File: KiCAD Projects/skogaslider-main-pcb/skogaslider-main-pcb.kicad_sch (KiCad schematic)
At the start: 172 parts, among them J1 USB_C_Receptacle_USB2.0, J2 USB_C_Receptacle_USB2.0, J3 Conn_01x05, J4 Conn_02x16_Top_Bottom, J5 Conn_01x09, J6 Conn_01x09, J7 Conn_01x04, J8 Conn_01x04, Q1 BSS138, SW1 SW_Push, SW2 SW_Push, SW3 SW_Push, SW4 SW_Push, U1 AMS1117-3.3, U2 MPR121QR2, U3 MPR121QR2, U4 USBLC6-2P6, U5 RP2040, U6 M24C02-RMN, U7 W25Q128JVS, U8 MPR121QR2, U9 74HC4051, Y1 ABLS-12.000MHZ-B4-T

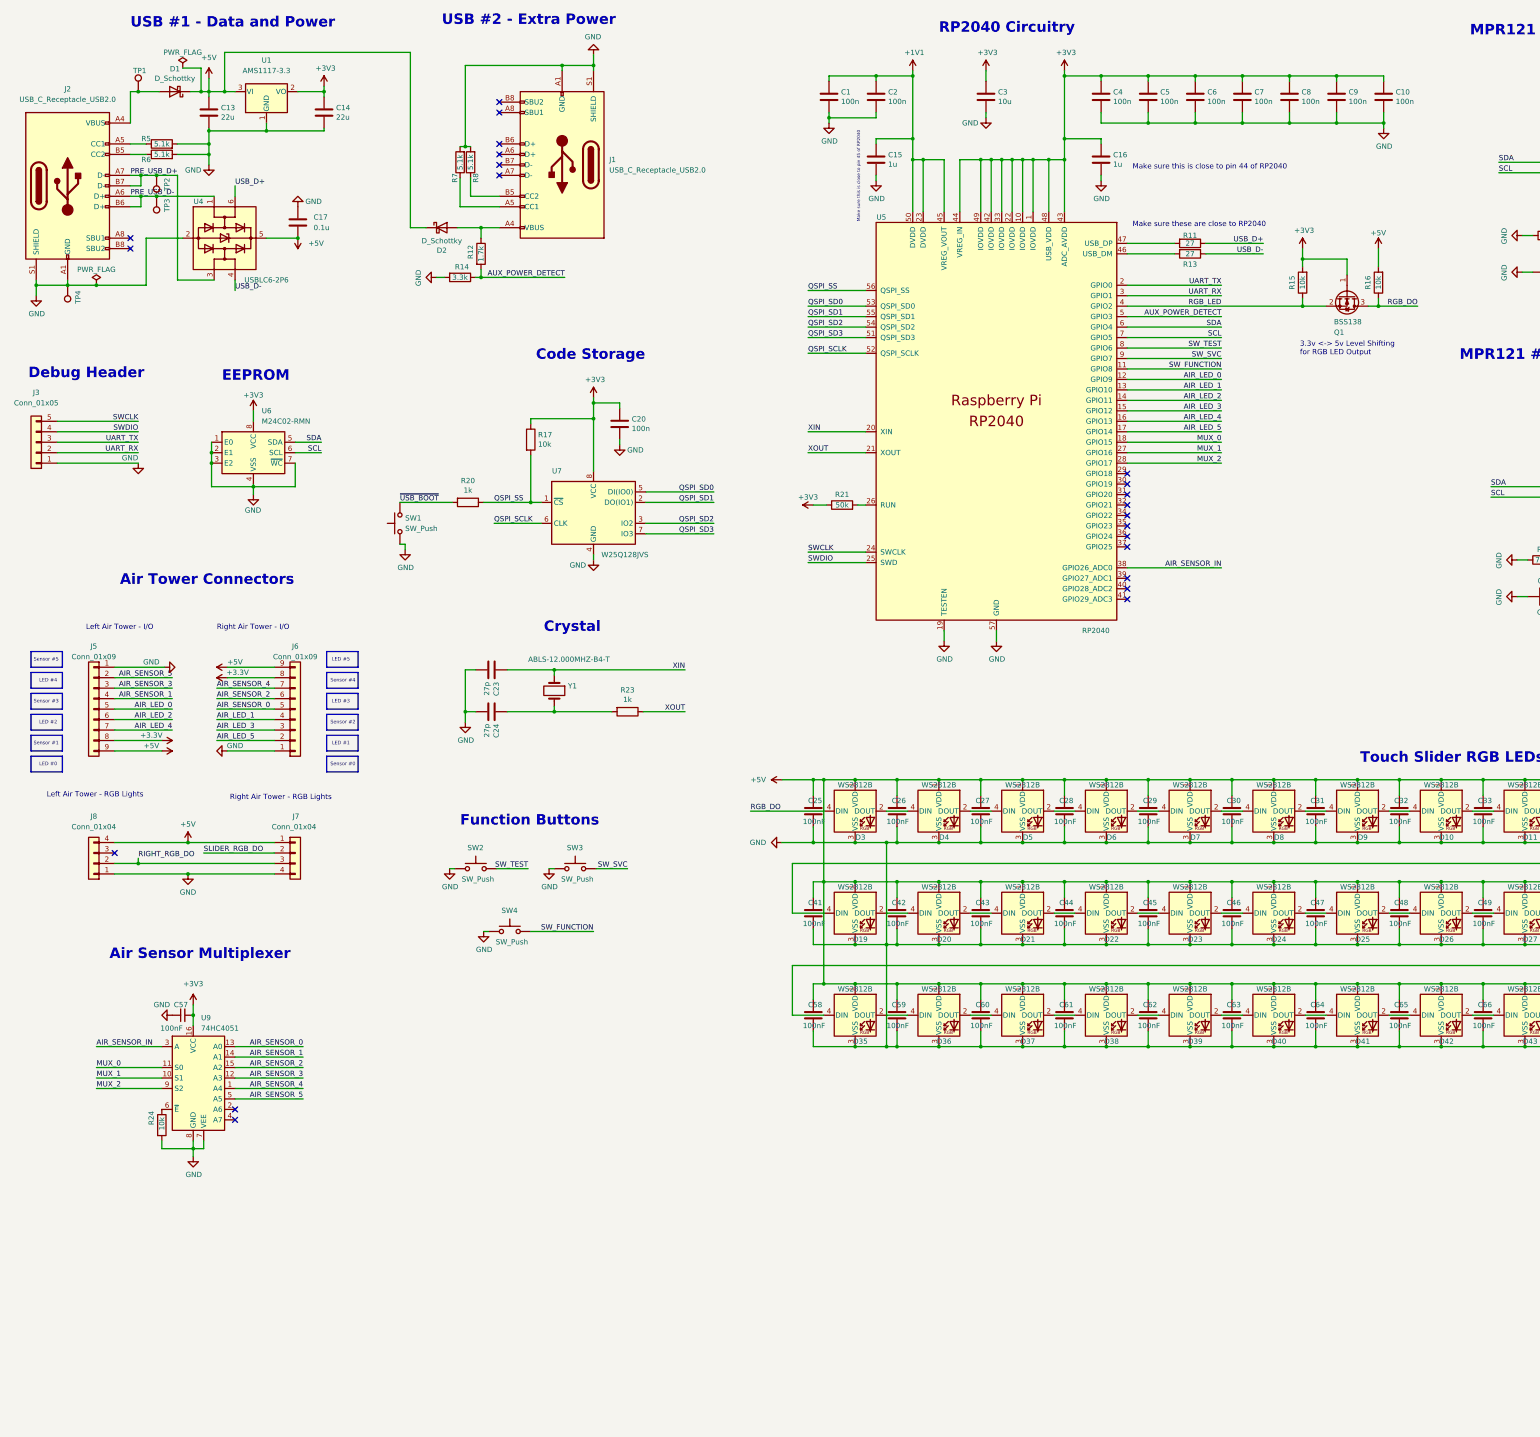
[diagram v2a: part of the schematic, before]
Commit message: PCB layout is almost complete for the mainboard, minus the board cuts, mounting holes, and power/ground planes
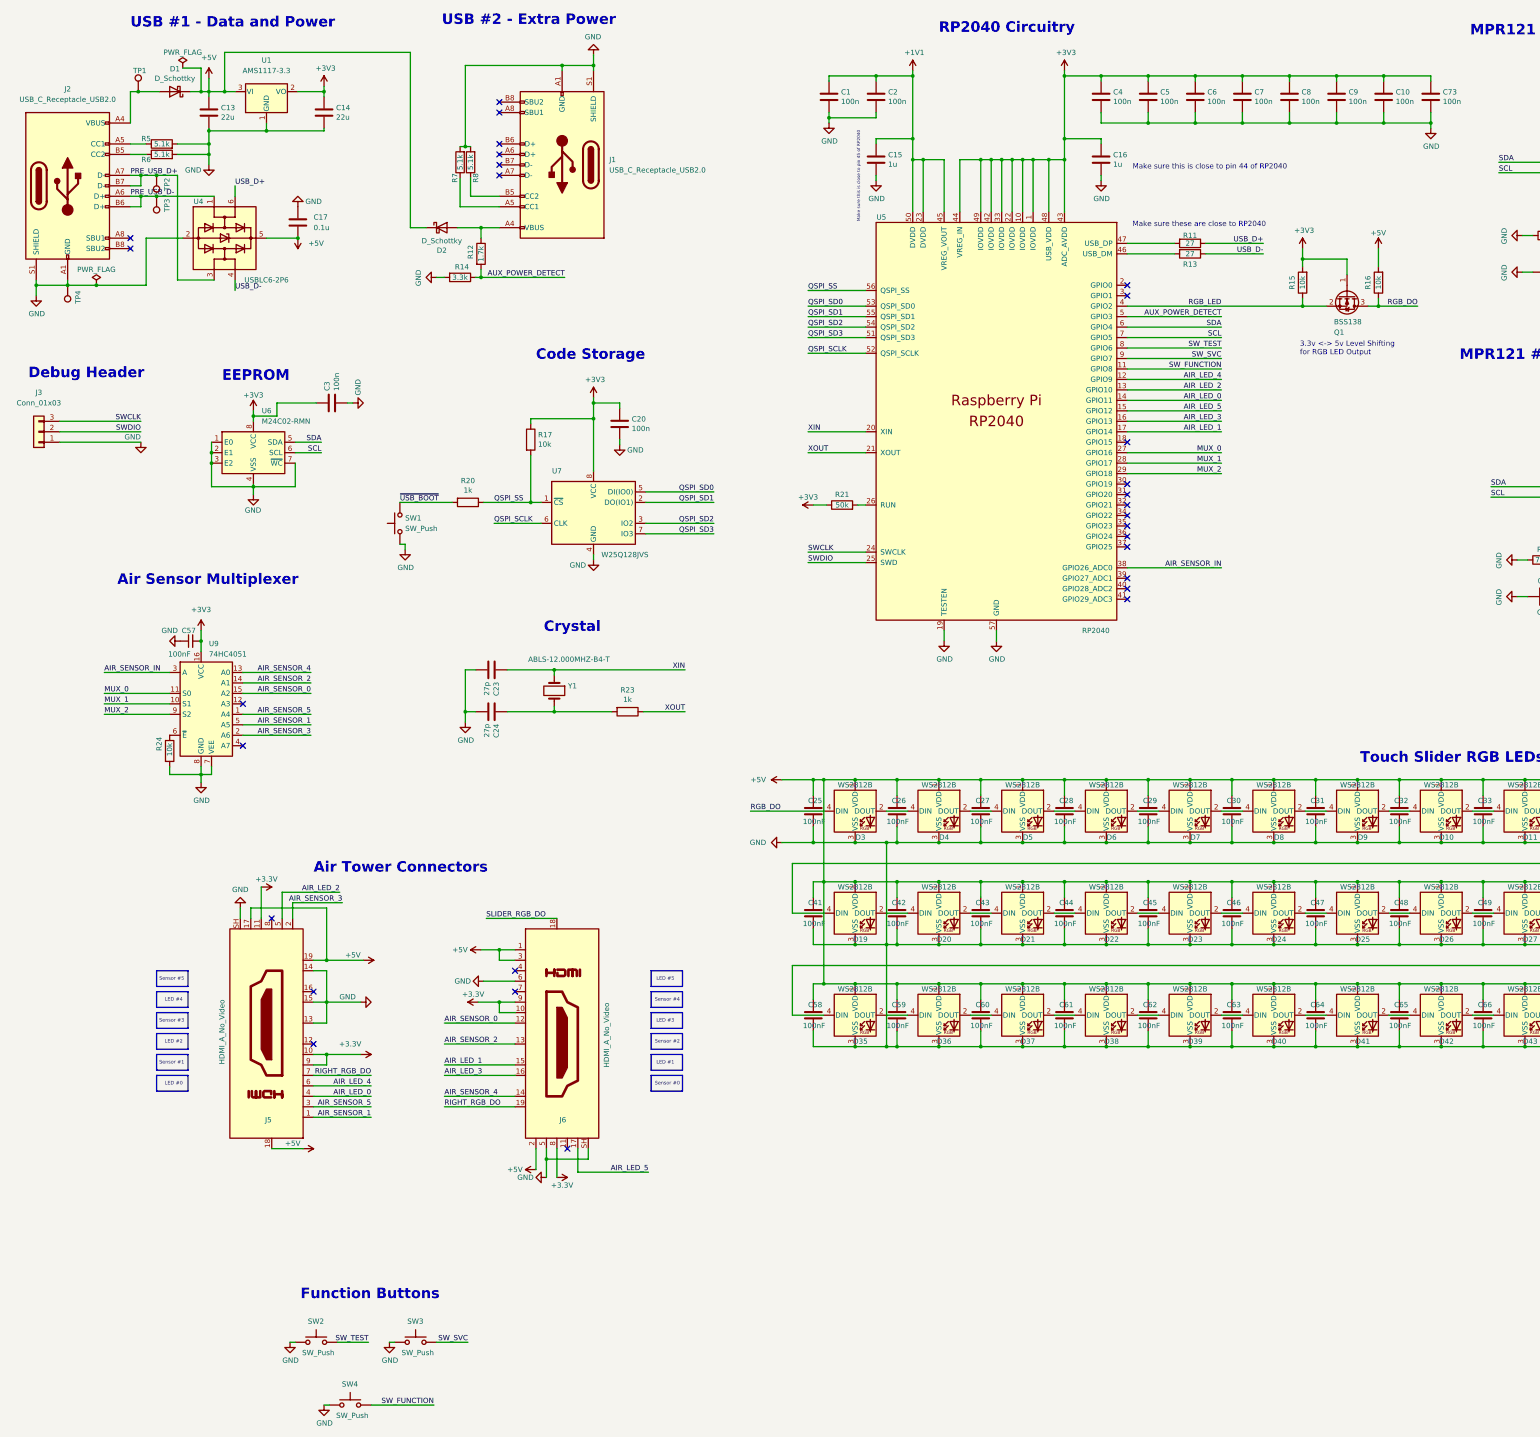
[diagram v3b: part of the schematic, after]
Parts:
- removed J3: Conn_01x05, Connector_PinHeader_2.54mm:PinHeader_1x05_P2.54mm_Vertical, symbol Connector_Generic:Conn_01x05
- removed J5, J6: Conn_01x09, Connector_JST:JST_PH_S9B-PH-K_1x09_P2.00mm_Horizontal, symbol Connector_Generic:Conn_01x09
- removed J7, J8: Conn_01x04, Connector_JST:JST_PH_S4B-PH-K_1x04_P2.00mm_Horizontal, symbol Connector_Generic:Conn_01x04
- added C73: 100n, Capacitor_SMD:C_0201_0603Metric, symbol Device:C
- added J3: Conn_01x03, Connector_PinHeader_2.54mm:PinHeader_1x03_P2.54mm_Vertical, symbol Connector_Generic:Conn_01x03
- added J5, J6: HDMI_A_No_Video, Skogaslider_Custom_Footprints:HDMI_Connector_SMD, symbol Skogaslider_Custom_Symbols:HDMI_A_No_Video
- C1, C10, C15, C16, C2, C4, C5, C6, C7, C8, C9: footprint Capacitor_SMD:C_0402_1005Metric -> Capacitor_SMD:C_0201_0603Metric
- C3: value 10u -> 100n; footprint Capacitor_SMD:C_0805_2012Metric -> Capacitor_SMD:C_0201_0603Metric
- R20: footprint Resistor_SMD:R_0402_1005Metric -> Resistor_SMD:R_0603_1608Metric
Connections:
- net +3V3: now also C73.1, J5.10, J5.11, J5.9, J6.10, J6.8, J6.9
- net +5V: now also J5.17, J5.18, J5.19, J6.1, J6.2, J6.3
- net AIR_LED_0: now also U5.14 (GPIO11), J5.4; no longer U5.12 (GPIO9)
- net AIR_LED_1: now also U5.17 (GPIO14), J6.15; no longer U5.13 (GPIO10)
- net AIR_LED_2: now also U5.13 (GPIO10), J5.5; no longer U5.14 (GPIO11)
- net AIR_LED_3: now also U5.16 (GPIO13), J6.16; no longer U5.15 (GPIO12)
- net AIR_LED_4: now also U5.12 (GPIO9), J5.6; no longer U5.16 (GPIO13)
- net AIR_LED_5: now also U5.15 (GPIO12), J6.17; no longer U5.17 (GPIO14)
- net AIR_SENSOR_0: now also U9.15 (A2), J6.12; no longer U9.13 (A0)
- net AIR_SENSOR_1: now also U9.5 (A5), J5.1; no longer U9.14 (A1)
- net AIR_SENSOR_2: now also U9.14 (A1), J6.13; no longer U9.15 (A2)
- net AIR_SENSOR_3: now also U9.2 (A6), J5.2; no longer U9.12 (A3)
- net AIR_SENSOR_4: now also U9.13 (A0), J6.14; no longer U9.1 (A4)
- net AIR_SENSOR_5: now also U9.1 (A4), J5.3; no longer U9.5 (A5)
- net GND: now also C73.2, J3.1 (Pin_1), J5.13, J5.14, J5.15, J5.SH, J6.5, J6.6, J6.SH
- net MUX_0: now also U5.27 (GPIO16); no longer U5.18 (GPIO15)
- net MUX_1: now also U5.28 (GPIO17); no longer U5.27 (GPIO16)
- net MUX_2: now also U5.29 (GPIO18); no longer U5.28 (GPIO17)
- net RIGHT_RGB_DO: now also J5.7, J6.19
- net SLIDER_RGB_DO: now also J6.18
- net SWCLK: now also J3.3 (Pin_3)
- net SWDIO: now also J3.2 (Pin_2)
- net UART_RX: no longer names the net of U5.3 (GPIO1)
- net UART_TX: no longer names the net of U5.2 (GPIO0)
- no-connect marks 29 -> 36
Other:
- note removed: "Left Air Tower - I/O"
- note removed: "Left Air Tower - RGB Lights"
- note removed: "Right Air Tower - I/O"
- note removed: "Right Air Tower - RGB Lights"
- moved on the sheet: C57, R24, SW2, SW3, SW4, U9

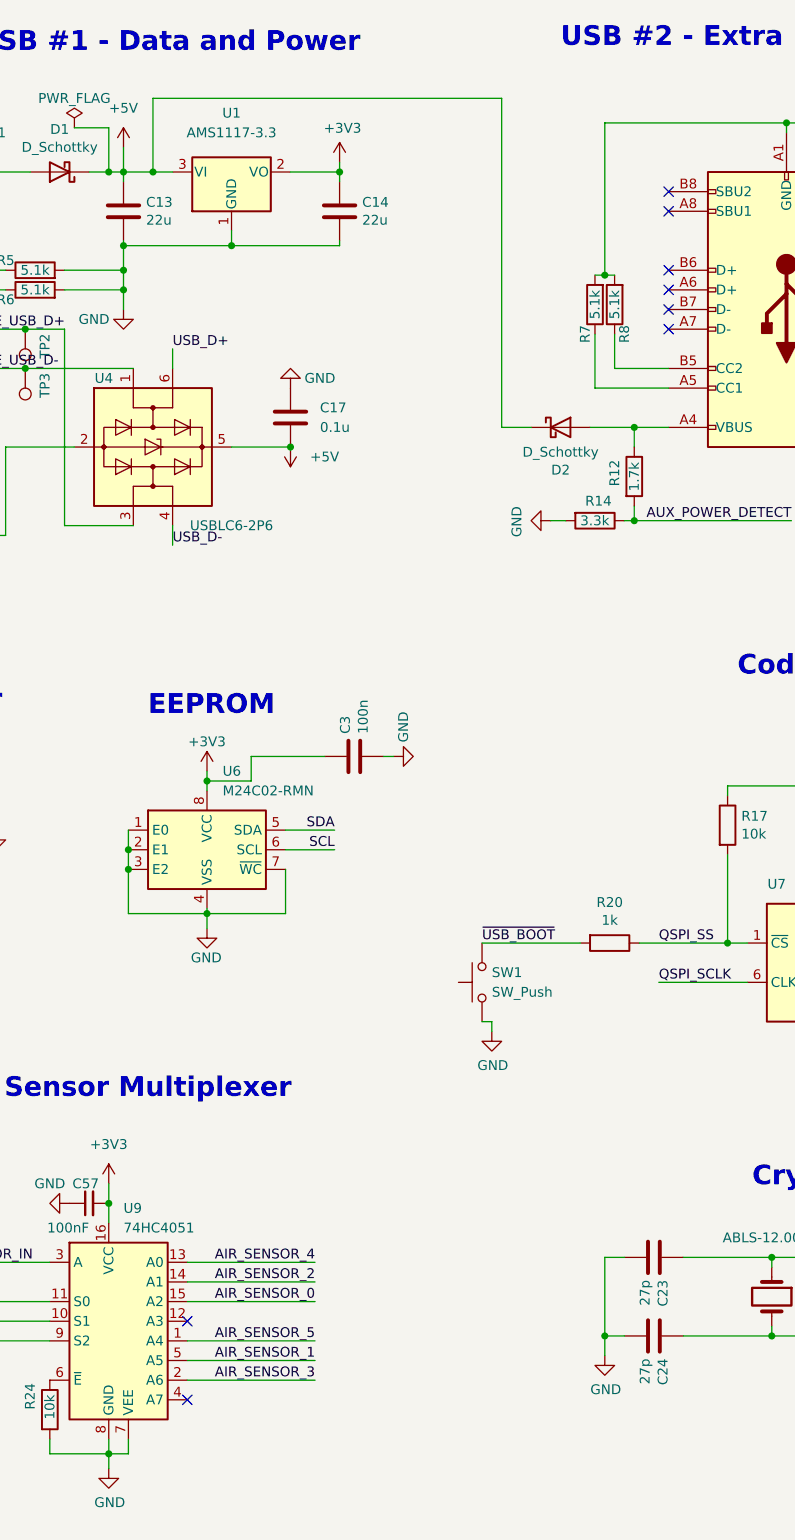
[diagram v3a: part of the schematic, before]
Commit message: Added JLCPCB part number mappings for everything, so we can export this via the jlcpcb plugin to order, once everything is finalized.
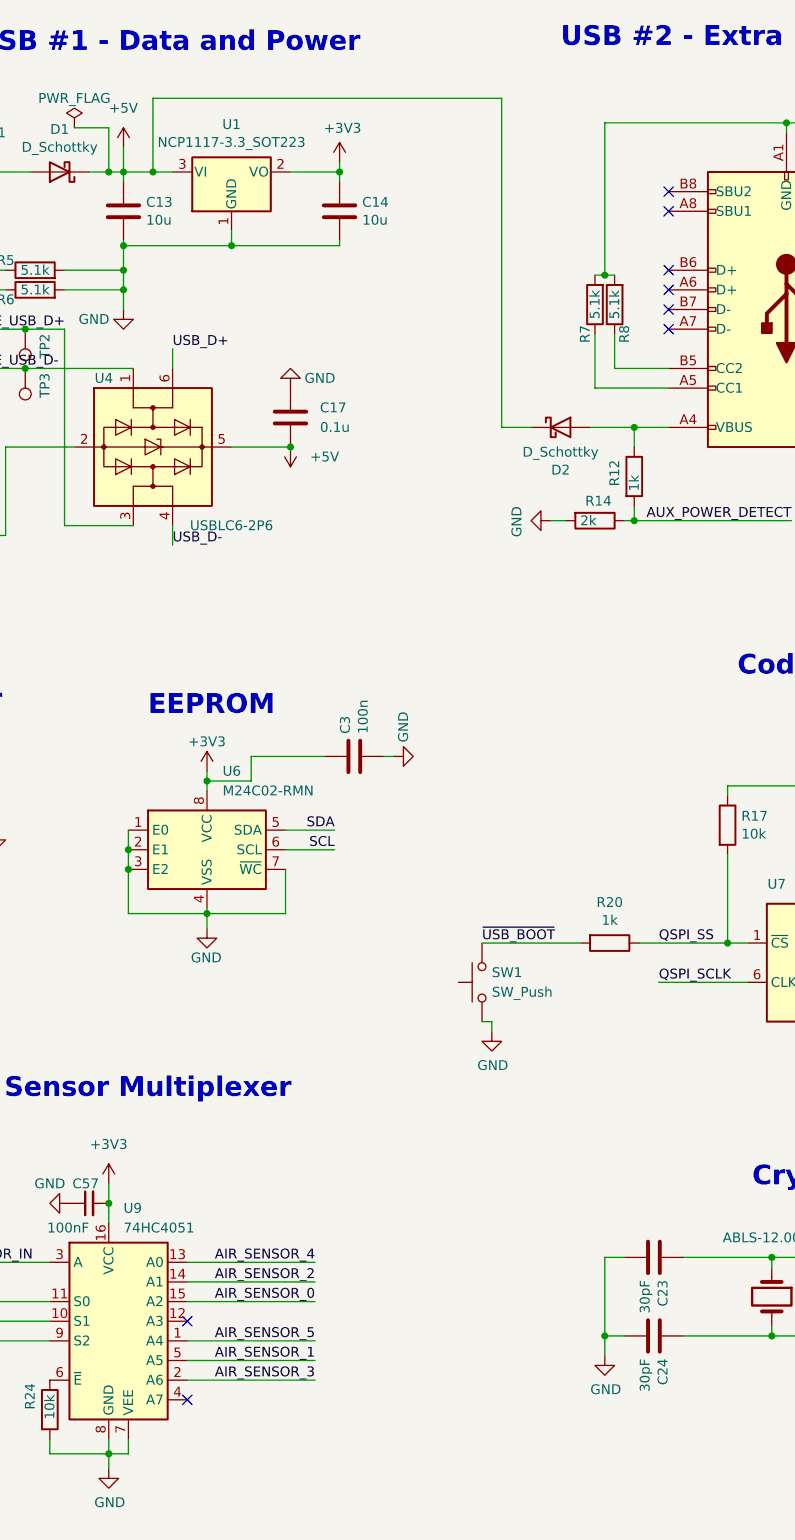
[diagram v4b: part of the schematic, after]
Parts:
- removed U1: AMS1117-3.3, Package_TO_SOT_SMD:SOT-223-3_TabPin2, symbol Regulator_Linear:AMS1117-3.3
- added U1: NCP1117-3.3_SOT223, Package_TO_SOT_SMD:SOT-223-3_TabPin2, symbol Regulator_Linear:NCP1117-3.3_SOT223
- C1, C10, C15, C16, C2, C3, C4, C5, C6, C7, C73, C8, C9: footprint Capacitor_SMD:C_0201_0603Metric -> Capacitor_SMD:C_0402_1005Metric
- C13, C14: value 22u -> 10u; footprint Capacitor_Tantalum_SMD:CP_EIA-1608-08_AVX-J -> Capacitor_SMD:C_0805_2012Metric
- C23, C24: value 27p -> 30pF
- C57: footprint Capacitor_SMD:C_0603_1608Metric -> Capacitor_SMD:C_0402_1005Metric
- R12: value 1.7k -> 1k
- R14: value 3.3k -> 2k
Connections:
- net +3V3: now also U1.2 (VO)
- net +5V: now also U1.3 (VI)
- net GND: now also U1.1 (GND)

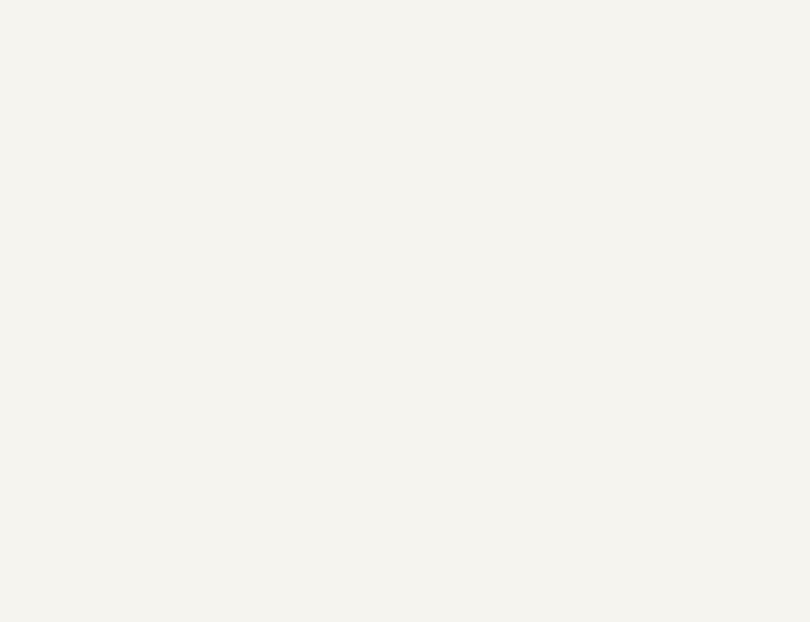
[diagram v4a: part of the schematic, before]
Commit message: v0.1 of the slider PCB is likely complete, waiting for a prototype order to arrive before making any real changes.
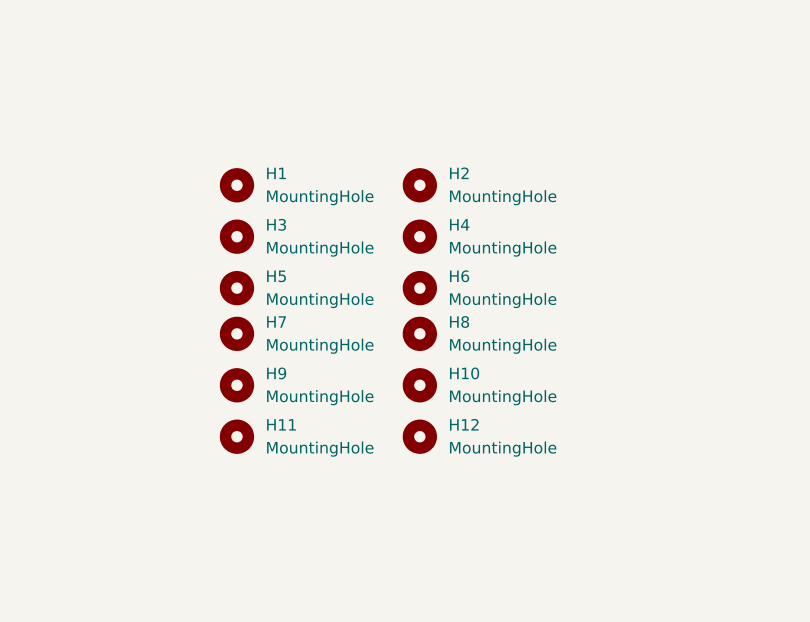
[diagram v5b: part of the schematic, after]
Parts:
- added H1, H10, H11, H12, H2, H3, H4, H5, H6, H7, H8, H9: MountingHole, MountingHole:MountingHole_3.2mm_M3, symbol Mechanical:MountingHole
